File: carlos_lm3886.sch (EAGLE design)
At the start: 17 parts

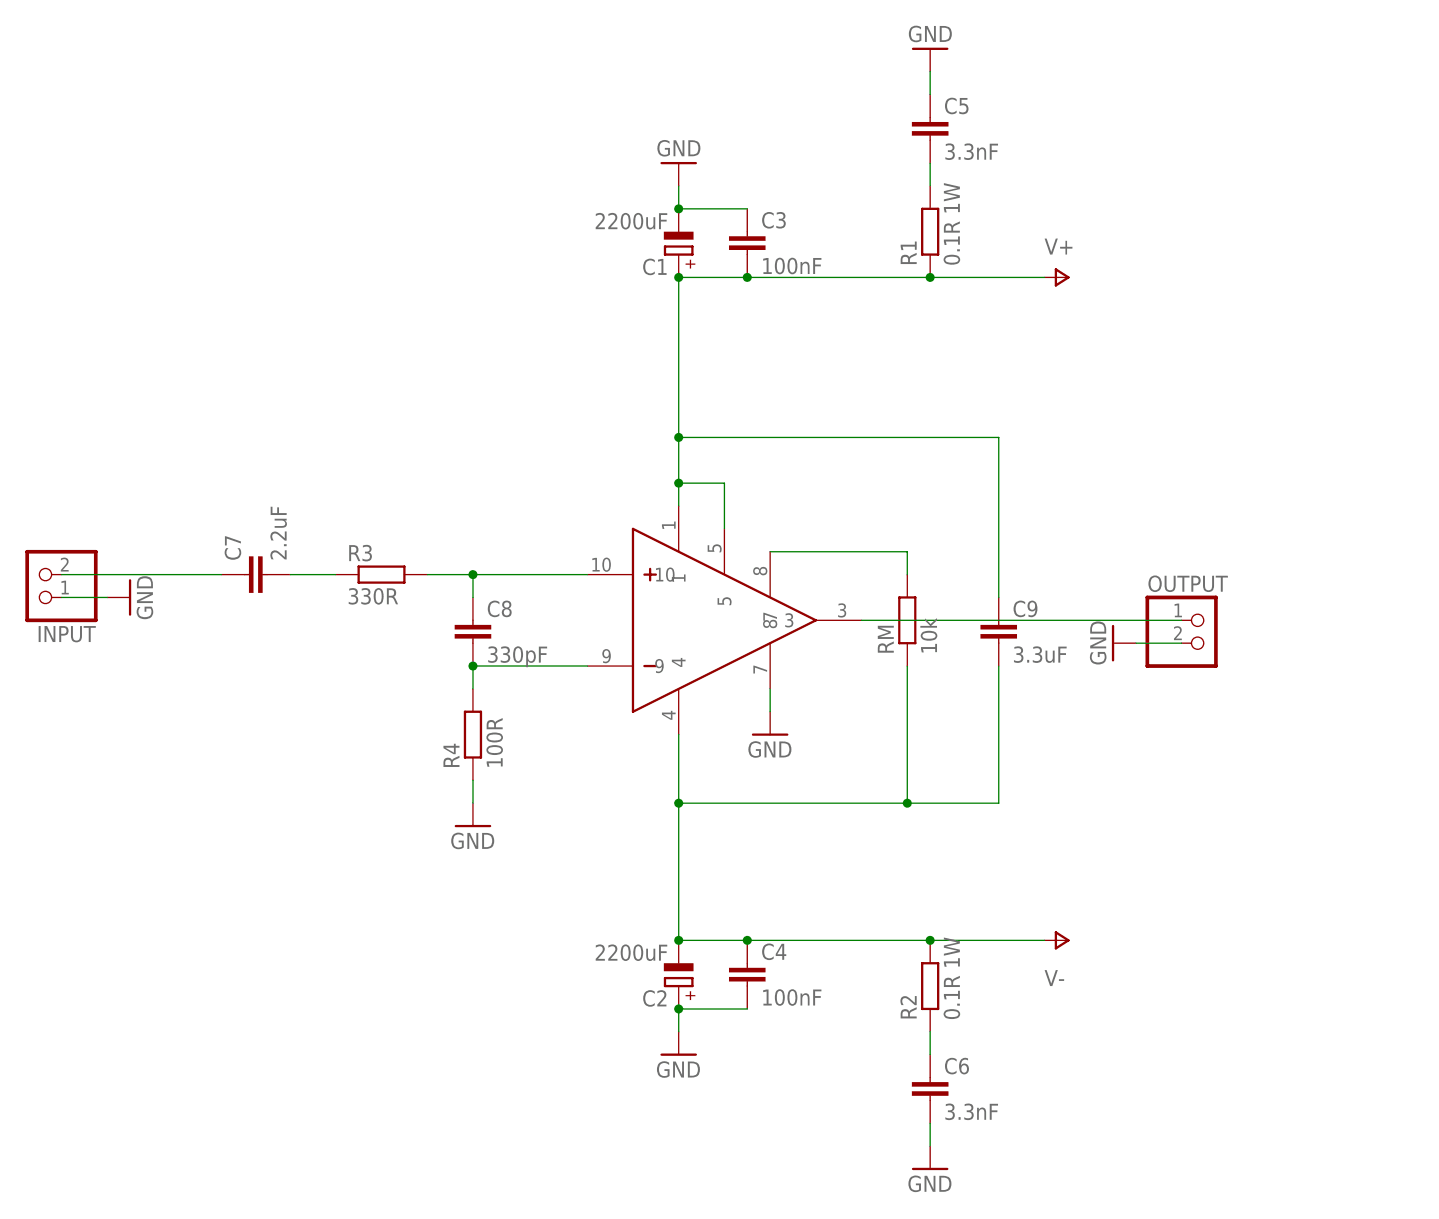
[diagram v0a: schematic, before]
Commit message: layout without traces completed
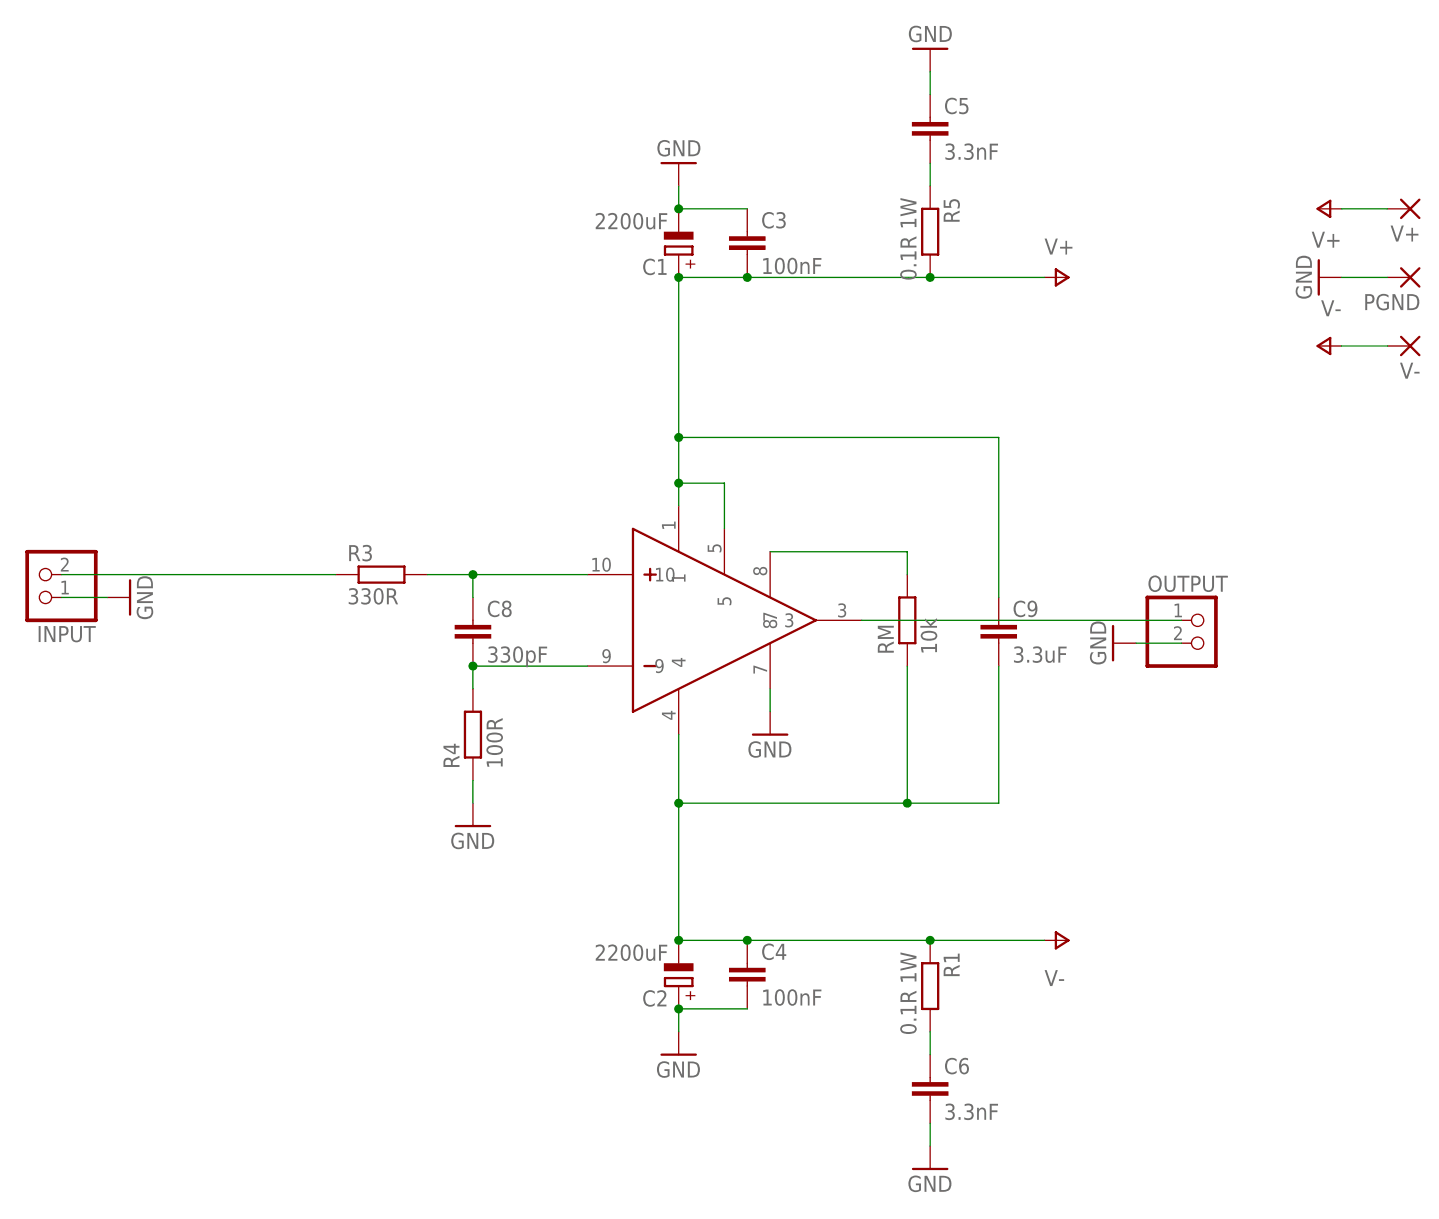
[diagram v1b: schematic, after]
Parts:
- removed C7: 2.2uF, rcl:C-EU225-087X268
- removed R2: 0.1R 1W, rcl:R-EU_0411/12
- added PGND, V+, V-: (no value), wirepad:2,54/1,0
- added R5: 0.1R 1W, resistor:R-EU_0309/10
- R1: device rcl:R-EU_0411/12 -> resistor:R-EU_0309/10
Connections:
- removed net N$2: C7.2, R3.1
- net GND: now also PGND.P
- net N$1: now also R3.1; no longer C7.1
- net N$3: now also R1.2; no longer R2.1
- net N$4: now also R5.1; no longer R1.2
- net V+: now also R5.2, V+.P; no longer R1.1
- net V-: now also R1.1, V-.P; no longer R2.2
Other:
- moved on the sheet: R1
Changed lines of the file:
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@@
 <layer number="97" name="Info" color="7" fill="1" visible="yes" active="yes"/>
 <layer number="98" name="Guide" color="6" fill="1" visible="yes" active="yes"/>
+<layer number="99" name="SpiceOrder" color="5" fill="1" visible="yes" active="yes"/>
 </layers>
 <schematic xreflabel="%F%N/%S.%C%R" xrefpart="/%S.%C%R">
@@
 <part name="C5" library="rcl" deviceset="C-EU" device="075-032X103" value="3.3nF"/>
 <part name="C6" library="rcl" deviceset="C-EU" device="075-032X103" value="3.3nF"/>
-<part name="R1" library="rcl" deviceset="R-EU_" device="0411/12" value="0.1R 1W"/>
-<part name="R2" library="rcl" deviceset="R-EU_" device="0411/12" value="0.1R 1W"/>
 <part name="GND3" library="supply1" deviceset="GND" device=""/>
 <part name="GND4" library="supply1" deviceset="GND" device=""/>
@@
 <part name="P-1" library="supply1" deviceset="V-" device=""/>
 <part name="GND5" library="supply1" deviceset="GND" device=""/>
-<part name="C7" library="rcl" deviceset="C-EU" device="225-087X268" value="2.2uF"/>
 <part name="INPUT" library="pinhead" deviceset="PINHD-1X2" device=""/>
 <part name="R3" library="rcl" deviceset="R-EU_" device="0207/10" value="330R"/>
@@
 <part name="RM" library="rcl" deviceset="R-EU_" device="0207/10" value="10k"/>
 <part name="C9" library="rcl" deviceset="C-EU" device="225-087X268" value="3.3uF"/>
+<part name="P+2" library="supply1" deviceset="V+" device=""/>
+<part name="P-2" library="supply1" deviceset="V-" device=""/>
+<part name="GND9" library="supply1" deviceset="GND" device=""/>
+<part name="R5" library="resistor" deviceset="R-EU_" device="0309/10" value="0.1R 1W"/>
+<part name="R1" library="resistor" deviceset="R-EU_" device="0309/10" value="0.1R 1W"/>
+<part name="V-" library="wirepad" deviceset="2,54/1,0" device=""/>
+<part name="PGND" library="wirepad" deviceset="2,54/1,0" device=""/>
+<part name="V+" library="wirepad" deviceset="2,54/1,0" device=""/>
 </parts>
 <sheets>
@@
 <instance part="C5" gate="G$1" x="93.98" y="109.22"/>
 <instance part="C6" gate="G$1" x="93.98" y="2.54"/>
-<instance part="R1" gate="G$1" x="93.98" y="96.52" rot="R90"/>
-<instance part="R2" gate="G$1" x="93.98" y="12.7" rot="R90"/>
 <instance part="GND3" gate="1" x="93.98" y="-7.62"/>
 <instance part="GND4" gate="1" x="93.98" y="116.84" rot="R180"/>
@@
 <instance part="P-1" gate="1" x="109.22" y="17.78" rot="R90"/>
 <instance part="GND5" gate="1" x="76.2" y="40.64"/>
-<instance part="C7" gate="G$1" x="17.78" y="58.42" rot="R90"/>
 <instance part="INPUT" gate="G$1" x="-5.08" y="58.42" rot="R180"/>
 <instance part="R3" gate="G$1" x="33.02" y="58.42"/>
@@
 <instance part="RM" gate="G$1" x="91.44" y="53.34" rot="R90"/>
 <instance part="C9" gate="G$1" x="101.6" y="53.34"/>
+<instance part="P+2" gate="1" x="137.16" y="99.06" rot="R90"/>
+<instance part="P-2" gate="1" x="137.16" y="83.82" rot="R270"/>
+<instance part="GND9" gate="1" x="137.16" y="91.44" rot="R270"/>
+<instance part="R5" gate="G$1" x="93.98" y="96.52" rot="R270"/>
+<instance part="R1" gate="G$1" x="93.98" y="12.7" rot="R270"/>
+<instance part="V-" gate="P" x="147.32" y="83.82" rot="R180"/>
+<instance part="PGND" gate="P" x="147.32" y="91.44" rot="R180"/>
+<instance part="V+" gate="P" x="147.32" y="99.06" rot="R180"/>
 </instances>
 <busses>
@@
 <wire x1="116.84" y1="50.8" x2="121.92" y2="50.8" width="0.1524" layer="91"/>
 </segment>
+<segment>
+<pinref part="GND9" gate="1" pin="GND"/>
+<pinref part="PGND" gate="P" pin="P"/>
+<wire x1="139.7" y1="91.44" x2="144.78" y2="91.44" width="0.1524" layer="91"/>
+</segment>
 </net>
 <net name="N$3" class="0">
 <segment>
-<pinref part="R2" gate="G$1" pin="1"/>
 <pinref part="C6" gate="G$1" pin="1"/>
 <wire x1="93.98" y1="7.62" x2="93.98" y2="5.08" width="0.1524" layer="91"/>
+<pinref part="R1" gate="G$1" pin="2"/>
 </segment>
 </net>
@@
 <pinref part="C2" gate="G$1" pin="-"/>
 <wire x1="73.66" y1="17.78" x2="66.04" y2="17.78" width="0.1524" layer="91"/>
-<pinref part="R2" gate="G$1" pin="2"/>
 <wire x1="73.66" y1="17.78" x2="93.98" y2="17.78" width="0.1524" layer="91"/>
 <junction x="73.66" y="17.78"/>
 <pinref part="P-1" gate="1" pin="V-"/>
+<pinref part="U$1" gate="G$1" pin="4"/>
 <wire x1="93.98" y1="17.78" x2="106.68" y2="17.78" width="0.1524" layer="91"/>
-<junction x="93.98" y="17.78"/>
-<pinref part="U$1" gate="G$1" pin="4"/>
 <wire x1="66.04" y1="40.64" x2="66.04" y2="33.02" width="0.1524" layer="91"/>
 <junction x="66.04" y="17.78"/>
@@
 <wire x1="101.6" y1="33.02" x2="91.44" y2="33.02" width="0.1524" layer="91"/>
 <junction x="91.44" y="33.02"/>
+<pinref part="R1" gate="G$1" pin="1"/>
+<junction x="93.98" y="17.78"/>
+</segment>
+<segment>
+<pinref part="P-2" gate="1" pin="V-"/>
+<pinref part="V-" gate="P" pin="P"/>
+<wire x1="139.7" y1="83.82" x2="144.78" y2="83.82" width="0.1524" layer="91"/>
 </segment>
 </net>
@@
 <segment>
 <pinref part="P+1" gate="1" pin="V+"/>
-<pinref part="R1" gate="G$1" pin="1"/>
-<wire x1="106.68" y1="91.44" x2="93.98" y2="91.44" width="0.1524" layer="91"/>
 <pinref part="C3" gate="G$1" pin="2"/>
 <pinref part="C1" gate="G$1" pin="+"/>
 <wire x1="73.66" y1="91.44" x2="66.04" y2="91.44" width="0.1524" layer="91"/>
-<wire x1="93.98" y1="91.44" x2="73.66" y2="91.44" width="0.1524" layer="91"/>
-<junction x="93.98" y="91.44"/>
+<wire x1="106.68" y1="91.44" x2="93.98" y2="91.44" width="0.1524" layer="91"/>
 <junction x="73.66" y="91.44"/>
 <pinref part="U$1" gate="G$1" pin="1"/>
+<wire x1="93.98" y1="91.44" x2="73.66" y2="91.44" width="0.1524" layer="91"/>
 <wire x1="66.04" y1="91.44" x2="66.04" y2="73.66" width="0.1524" layer="91"/>
 <junction x="66.04" y="91.44"/>
@@
 <wire x1="101.6" y1="73.66" x2="66.04" y2="73.66" width="0.1524" layer="91"/>
 <junction x="66.04" y="73.66"/>
+<pinref part="R5" gate="G$1" pin="2"/>
+<junction x="93.98" y="91.44"/>
+</segment>
+<segment>
+<pinref part="P+2" gate="1" pin="V+"/>
+<pinref part="V+" gate="P" pin="P"/>
+<wire x1="139.7" y1="99.06" x2="144.78" y2="99.06" width="0.1524" layer="91"/>
 </segment>
 </net>
 <net name="N$4" class="0">
 <segment>
-<pinref part="R1" gate="G$1" pin="2"/>
 <pinref part="C5" gate="G$1" pin="2"/>
 <wire x1="93.98" y1="101.6" x2="93.98" y2="104.14" width="0.1524" layer="91"/>
+<pinref part="R5" gate="G$1" pin="1"/>
 </segment>
 </net>
@@
 <segment>
 <pinref part="INPUT" gate="G$1" pin="2"/>
-<pinref part="C7" gate="G$1" pin="1"/>
-<wire x1="-2.54" y1="58.42" x2="15.24" y2="58.42" width="0.1524" layer="91"/>
-</segment>
-</net>
-<net name="N$2" class="0">
-<segment>
-<pinref part="C7" gate="G$1" pin="2"/>
+<wire x1="-2.54" y1="58.42" x2="27.94" y2="58.42" width="0.1524" layer="91"/>
 <pinref part="R3" gate="G$1" pin="1"/>
-<wire x1="22.86" y1="58.42" x2="27.94" y2="58.42" width="0.1524" layer="91"/>
-</segment>
-</net>
+</segment>
+</net>

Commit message: final?
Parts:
- removed OUTPUT: (no value), pinhead:PINHD-1X2
- removed RM: 10k, rcl:R-EU_0207/10
- added A1, A2, CHASSIS, OUT+, OUT-: (no value), wirepad:2,54/1,0
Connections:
- removed net N$8: RM.2, U$1.8
- net GND: now also A1.P, A2.P, CHASSIS.P, OUT-.P; no longer OUTPUT.2
- net N$7: now also OUT+.P; no longer OUTPUT.1
- net V-: no longer RM.1
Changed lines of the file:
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@@
 <part name="R4" library="rcl" deviceset="R-EU_" device="0207/10" value="100R"/>
 <part name="GND6" library="supply1" deviceset="GND" device=""/>
-<part name="OUTPUT" library="pinhead" deviceset="PINHD-1X2" device=""/>
 <part name="GND7" library="supply1" deviceset="GND" device=""/>
 <part name="GND8" library="supply1" deviceset="GND" device=""/>
-<part name="RM" library="rcl" deviceset="R-EU_" device="0207/10" value="10k"/>
 <part name="C9" library="rcl" deviceset="C-EU" device="225-087X268" value="3.3uF"/>
 <part name="P+2" library="supply1" deviceset="V+" device=""/>
@@
 <part name="PGND" library="wirepad" deviceset="2,54/1,0" device=""/>
 <part name="V+" library="wirepad" deviceset="2,54/1,0" device=""/>
+<part name="OUT+" library="wirepad" deviceset="2,54/1,0" device=""/>
+<part name="OUT-" library="wirepad" deviceset="2,54/1,0" device=""/>
+<part name="A1" library="wirepad" deviceset="2,54/1,0" device=""/>
+<part name="A2" library="wirepad" deviceset="2,54/1,0" device=""/>
+<part name="GND10" library="supply1" deviceset="GND" device=""/>
+<part name="GND11" library="supply1" deviceset="GND" device=""/>
+<part name="CHASSIS" library="wirepad" deviceset="2,54/1,0" device=""/>
+<part name="GND12" library="supply1" deviceset="GND" device=""/>
 </parts>
 <sheets>
@@
 <instance part="R4" gate="G$1" x="43.18" y="40.64" rot="R90"/>
 <instance part="GND6" gate="1" x="43.18" y="30.48"/>
-<instance part="OUTPUT" gate="G$1" x="124.46" y="50.8"/>
 <instance part="GND7" gate="1" x="5.08" y="55.88" rot="R90"/>
-<instance part="GND8" gate="1" x="114.3" y="50.8" rot="R270"/>
-<instance part="RM" gate="G$1" x="91.44" y="53.34" rot="R90"/>
+<instance part="GND8" gate="1" x="114.3" y="45.72" rot="R270"/>
 <instance part="C9" gate="G$1" x="101.6" y="53.34"/>
 <instance part="P+2" gate="1" x="137.16" y="99.06" rot="R90"/>
@@
 <instance part="PGND" gate="P" x="147.32" y="91.44" rot="R180"/>
 <instance part="V+" gate="P" x="147.32" y="99.06" rot="R180"/>
+<instance part="OUT+" gate="P" x="124.46" y="53.34" rot="R180"/>
+<instance part="OUT-" gate="P" x="124.46" y="45.72" rot="R180"/>
+<instance part="A1" gate="P" x="10.16" y="101.6"/>
+<instance part="A2" gate="P" x="10.16" y="93.98"/>
+<instance part="GND10" gate="1" x="17.78" y="101.6" rot="R90"/>
+<instance part="GND11" gate="1" x="17.78" y="93.98" rot="R90"/>
+<instance part="CHASSIS" gate="P" x="10.16" y="109.22"/>
+<instance part="GND12" gate="1" x="17.78" y="109.22" rot="R90"/>
 </instances>
 <busses>
@@
 </segment>
 <segment>
-<pinref part="GND8" gate="1" pin="GND"/>
-<pinref part="OUTPUT" gate="G$1" pin="2"/>
-<wire x1="116.84" y1="50.8" x2="121.92" y2="50.8" width="0.1524" layer="91"/>
-</segment>
-<segment>
 <pinref part="GND9" gate="1" pin="GND"/>
 <pinref part="PGND" gate="P" pin="P"/>
 <wire x1="139.7" y1="91.44" x2="144.78" y2="91.44" width="0.1524" layer="91"/>
+</segment>
+<segment>
+<pinref part="GND8" gate="1" pin="GND"/>
+<pinref part="OUT-" gate="P" pin="P"/>
+<wire x1="116.84" y1="45.72" x2="121.92" y2="45.72" width="0.1524" layer="91"/>
+</segment>
+<segment>
+<pinref part="A1" gate="P" pin="P"/>
+<pinref part="GND10" gate="1" pin="GND"/>
+<wire x1="12.7" y1="101.6" x2="15.24" y2="101.6" width="0.1524" layer="91"/>
+</segment>
+<segment>
+<pinref part="A2" gate="P" pin="P"/>
+<pinref part="GND11" gate="1" pin="GND"/>
+<wire x1="12.7" y1="93.98" x2="15.24" y2="93.98" width="0.1524" layer="91"/>
+</segment>
+<segment>
+<pinref part="CHASSIS" gate="P" pin="P"/>
+<pinref part="GND12" gate="1" pin="GND"/>
+<wire x1="12.7" y1="109.22" x2="15.24" y2="109.22" width="0.1524" layer="91"/>
 </segment>
 </net>
@@
 <wire x1="66.04" y1="40.64" x2="66.04" y2="33.02" width="0.1524" layer="91"/>
 <junction x="66.04" y="17.78"/>
-<pinref part="RM" gate="G$1" pin="1"/>
 <wire x1="66.04" y1="33.02" x2="66.04" y2="17.78" width="0.1524" layer="91"/>
-<wire x1="91.44" y1="48.26" x2="91.44" y2="33.02" width="0.1524" layer="91"/>
-<wire x1="91.44" y1="33.02" x2="66.04" y2="33.02" width="0.1524" layer="91"/>
+<wire x1="101.6" y1="33.02" x2="66.04" y2="33.02" width="0.1524" layer="91"/>
 <junction x="66.04" y="33.02"/>
 <pinref part="C9" gate="G$1" pin="2"/>
 <wire x1="101.6" y1="48.26" x2="101.6" y2="33.02" width="0.1524" layer="91"/>
-<wire x1="101.6" y1="33.02" x2="91.44" y2="33.02" width="0.1524" layer="91"/>
-<junction x="91.44" y="33.02"/>
 <pinref part="R1" gate="G$1" pin="1"/>
 <junction x="93.98" y="17.78"/>
@@
 <segment>
 <pinref part="U$1" gate="G$1" pin="3"/>
-<pinref part="OUTPUT" gate="G$1" pin="1"/>
 <wire x1="86.36" y1="53.34" x2="121.92" y2="53.34" width="0.1524" layer="91"/>
-</segment>
-</net>
-<net name="N$8" class="0">
-<segment>
-<pinref part="U$1" gate="G$1" pin="8"/>
-<pinref part="RM" gate="G$1" pin="2"/>
-<wire x1="76.2" y1="60.96" x2="91.44" y2="60.96" width="0.1524" layer="91"/>
-<wire x1="91.44" y1="60.96" x2="91.44" y2="58.42" width="0.1524" layer="91"/>
-</segment>
-</net>
+<pinref part="OUT+" gate="P" pin="P"/>
+</segment>
+</net>
